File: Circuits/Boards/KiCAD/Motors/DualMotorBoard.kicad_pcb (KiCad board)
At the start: 2 copper layers, 127 x 101.6 mm, 124 parts, among them J1 Conn_01x05, J10 Conn_01x01, J11 Conn_01x01, J12 Conn_01x01, J13 Conn_01x01, J14 Conn_01x01, J15 Conn_01x02, J16 Conn_01x02, J17 MC34063, J2 Conn_01x01, J3 Conn_01x01, J4 Conn_01x01, J5 Conn_01x01, J6 Conn_01x01, J7 Conn_01x01, J8 Conn_01x05, J9 Conn_01x01, Q1 2N3904, Q10 Q_NMOS_DGS, Q11 Q_NMOS_DGS, Q12 Q_NMOS_DGS, Q13 Q_NMOS_DGS, Q14 2N3904, Q15 2N3904, Q16 2N3904, Q17 2N3904, Q18 2N3904, Q19 2N3904, Q2 2N3904, Q20 2N3904, Q21 2N3904, Q22 2N3904, Q23 Q_NMOS_DGS, Q24 Q_NMOS_DGS, Q25 Q_NMOS_DGS, Q26 Q_NMOS_DGS, Q3 2N3904, Q4 2N3904, Q5 2N3904, Q6 2N3904, Q7 2N3904, Q8 2N3904, Q9 2N3904, U2 LM7805_TO220

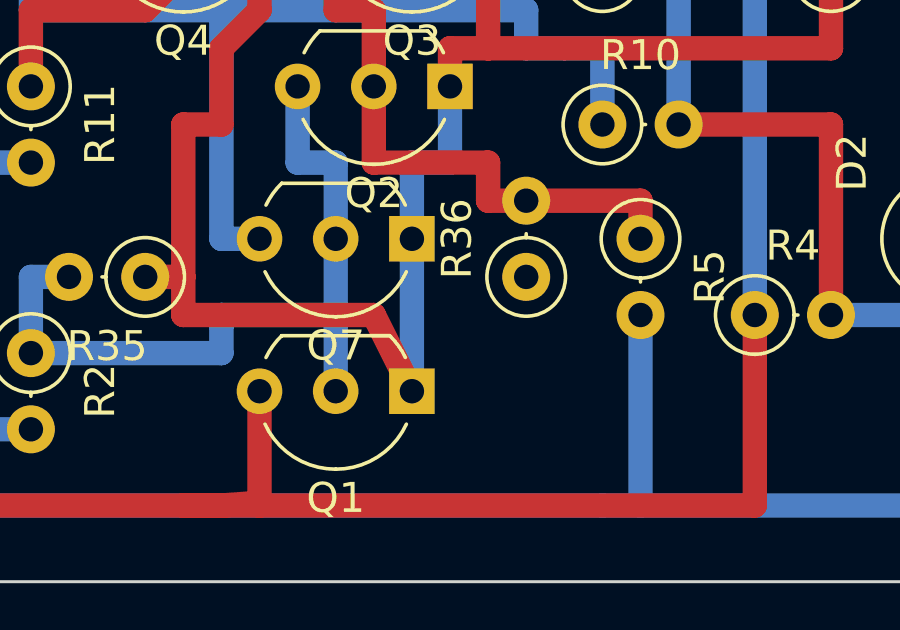
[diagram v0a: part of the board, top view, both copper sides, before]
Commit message: Fixed missing connections and routing errors
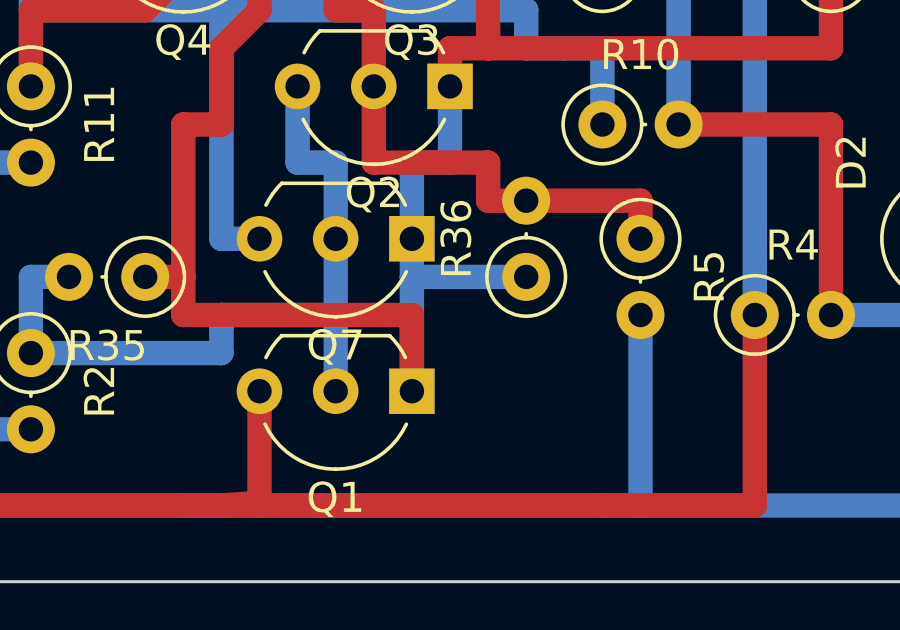
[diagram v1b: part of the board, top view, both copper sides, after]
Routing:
- net GND: track 605.8 -> 610.6 mm
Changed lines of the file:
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@@
   (general
     (links 255)
-    (no_connects 1)
+    (no_connects 0)
     (area 126.281 25.349999 254.819 127.549)
     (thickness 1.6)
     (drawings 4)
-    (tracks 543)
+    (tracks 546)
     (zones 0)
     (modules 124)
@@
   (segment (start 243.8 104.1) (end 242.57 102.87) (width 0.8128) (layer B.Cu) (net 1))
   (segment (start 250.19 101.6) (end 250.19 92.71) (width 0.8128) (layer B.Cu) (net 2))
+  (segment (start 223.52 118.11) (end 224.79 118.11) (width 0.8128) (layer F.Cu) (net 3))
+  (segment (start 224.79 118.11) (end 224.79 120.65) (width 0.8128) (layer F.Cu) (net 3))
+  (segment (start 228.6 116.84) (end 224.79 116.84) (width 0.8128) (layer B.Cu) (net 3))
   (segment (start 250.19 106.6) (end 238.84 106.6) (width 0.8128) (layer B.Cu) (net 3))
   (segment (start 238.84 106.6) (end 238.76 106.68) (width 0.8128) (layer B.Cu) (net 3))
@@
   (segment (start 215.9 116.84) (end 217.17 116.84) (width 0.8128) (layer F.Cu) (net 3))
   (segment (start 219.71 105.41) (end 219.71 107.95) (width 0.8128) (layer F.Cu) (net 3))
-  (segment (start 223.52 118.11) (end 224.79 120.65) (width 0.8128) (layer F.Cu) (net 3) (status 20))
   (segment (start 217.17 118.11) (end 223.52 118.11) (width 0.8128) (layer F.Cu) (net 3))
   (segment (start 217.17 111.76) (end 217.17 116.84) (width 0.8128) (layer F.Cu) (net 3))
@@
   (segment (start 218.44 109.22) (end 218.44 111.76) (width 0.8128) (layer F.Cu) (net 3))
   (segment (start 219.71 107.95) (end 218.44 109.22) (width 0.8128) (layer F.Cu) (net 3))
-  (segment (start 224.79 115.57) (end 224.79 120.65) (width 0.8128) (layer B.Cu) (net 3))
+  (segment (start 224.79 115.57) (end 224.79 116.84) (width 0.8128) (layer B.Cu) (net 3))
+  (segment (start 224.79 116.84) (end 224.79 120.65) (width 0.8128) (layer B.Cu) (net 3))
   (segment (start 214.63 62.23) (end 214.63 63.5) (width 0.8128) (layer B.Cu) (net 3))
   (segment (start 238.76 57.15) (end 247.65 57.15) (width 0.8128) (layer B.Cu) (net 3))
@@
   (segment (start 130.81 104.26) (end 137.04 104.26) (width 0.8128) (layer B.Cu) (net 48))
   (segment (start 137.04 104.26) (end 138.43 102.87) (width 0.8128) (layer B.Cu) (net 48))
-  (segment (start 201.93 116.84) (end 201.93 119.38) (width 1.27) (layer B.Cu) (net 49) (status 400000))
-  (segment (start 193.04 119.38) (end 193.04 121.92) (width 1.27) (layer B.Cu) (net 49) (status 800000))
+  (segment (start 201.93 116.84) (end 201.93 119.38) (width 1.27) (layer B.Cu) (net 49))
+  (segment (start 193.04 119.38) (end 193.04 121.92) (width 1.27) (layer B.Cu) (net 49))
   (segment (start 201.93 119.38) (end 193.04 119.38) (width 1.27) (layer B.Cu) (net 49))
-  (segment (start 195.54 121.92) (end 199.39 121.92) (width 1.27) (layer B.Cu) (net 50) (status C00000))
+  (segment (start 195.54 121.92) (end 199.39 121.92) (width 1.27) (layer B.Cu) (net 50))
   (segment (start 198.12 34.29) (end 198.12 34.29) (width 0.8128) (layer F.Cu) (net 51) (status 30))
   (segment (start 191.77 93.98) (end 194.31 93.98) (width 1.27) (layer F.Cu) (net 52))

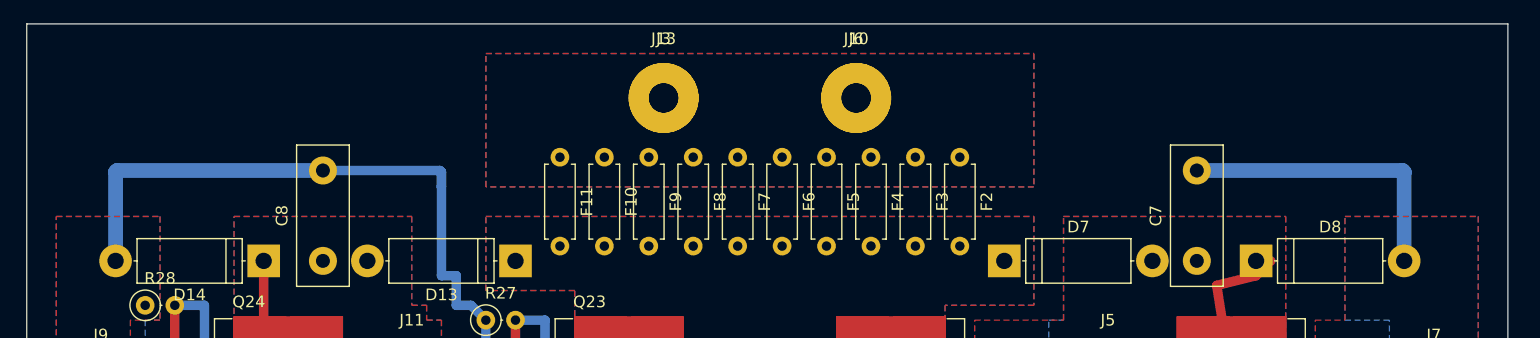
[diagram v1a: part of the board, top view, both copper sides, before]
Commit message: Added pin outputs for battery to ground (for external connections)
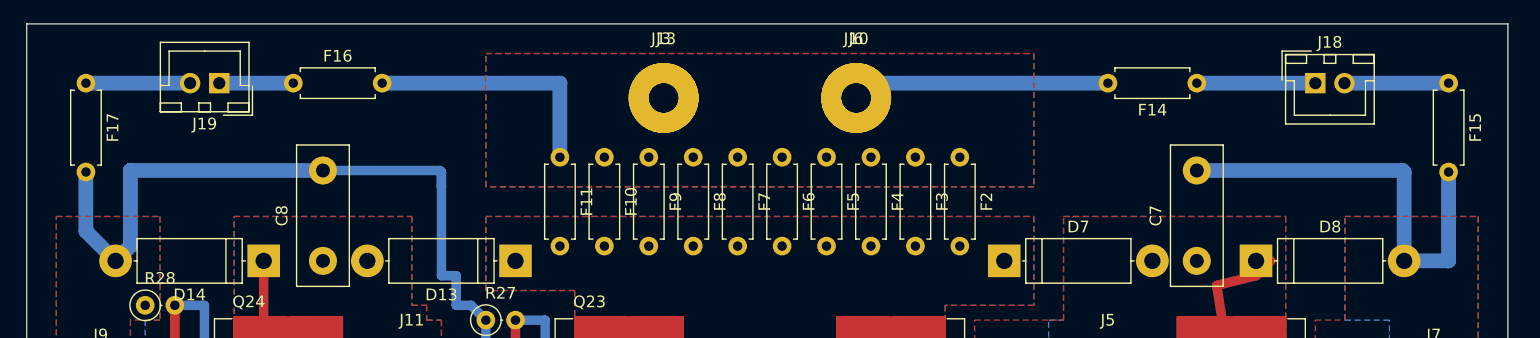
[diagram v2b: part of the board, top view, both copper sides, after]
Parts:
- added F14: Polyfuse, Resistors_THT:R_Axial_DIN0207_L6.3mm_D2.5mm_P7.62mm_Horizontal, F.Cu at (227.3, 30.5)
- added F15: Polyfuse, Resistors_THT:R_Axial_DIN0207_L6.3mm_D2.5mm_P7.62mm_Horizontal, F.Cu at (248.9, 30.5)
- added F16: Polyfuse, Resistors_THT:R_Axial_DIN0207_L6.3mm_D2.5mm_P7.62mm_Horizontal, F.Cu at (149.9, 30.5)
- added F17: Polyfuse, Resistors_THT:R_Axial_DIN0207_L6.3mm_D2.5mm_P7.62mm_Horizontal, F.Cu at (132.1, 30.5)
- added J18: Conn_01x02, Connectors_JST:JST_XH_B02B-XH-A_02x2.50mm_Straight, F.Cu at (237.5, 30.5)
- added J19: Conn_01x02, Connectors_JST:JST_XH_B02B-XH-A_02x2.50mm_Straight, F.Cu at (143.5, 30.5)
- C4: value 100uF -> 0.33uF
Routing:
- net +BATT: track 0.00 -> 43.7 mm
- net GND: track 610.6 -> 630.3 mm
- net Net-(F14-Pad1): track 0.00 -> 10.2 mm
- net Net-(F17-Pad1): track 0.00 -> 8.93 mm
- net Net-(F15-Pad1): track 0.00 -> 8.93 mm
- net Net-(F16-Pad1): track 0.00 -> 6.35 mm

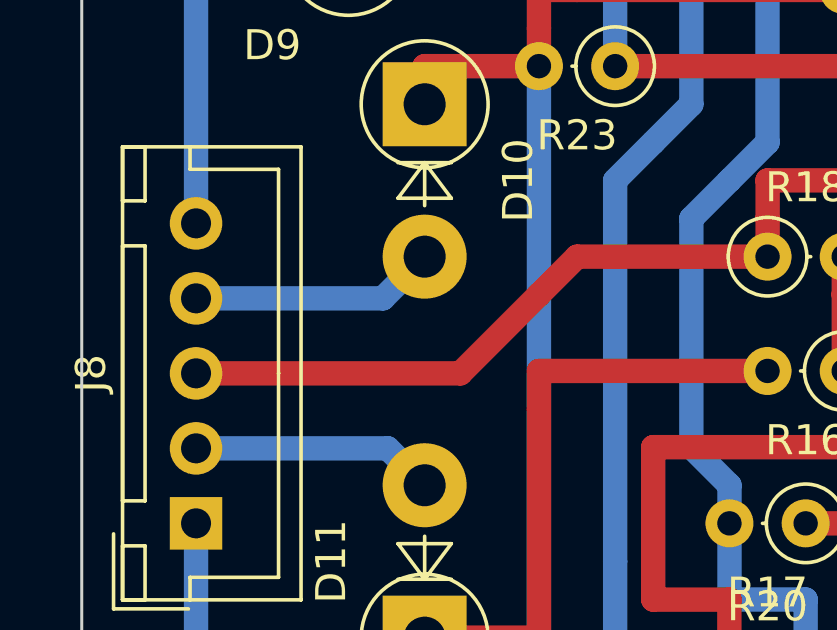
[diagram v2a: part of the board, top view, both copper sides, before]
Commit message: Transferred all JXT connections to bottomw traces
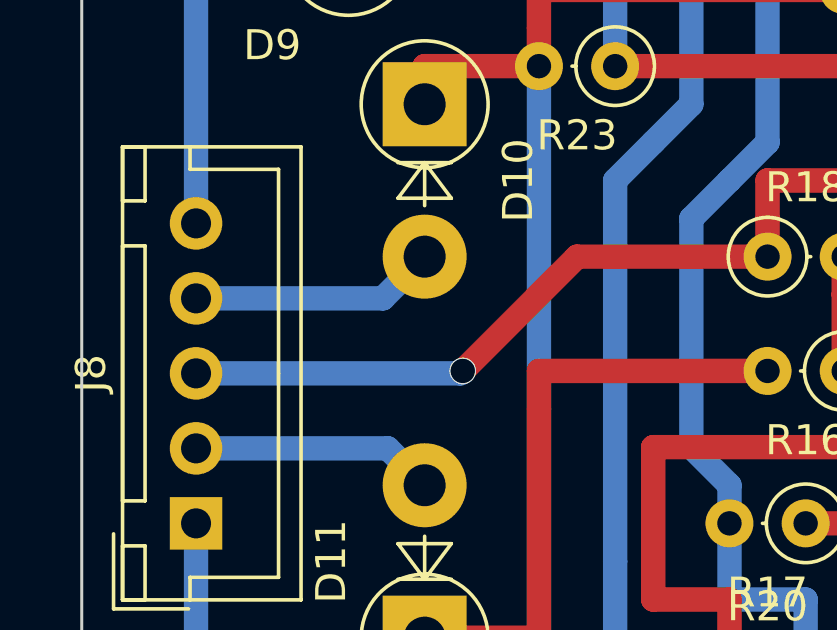
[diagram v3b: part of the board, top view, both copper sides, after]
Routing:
- net GND: vias 0 -> 1
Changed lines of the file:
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@@
     (thickness 1.6)
     (drawings 4)
-    (tracks 560)
+    (tracks 561)
     (zones 0)
     (modules 130)
@@
   (segment (start 243.8 104.1) (end 242.57 102.87) (width 0.8128) (layer B.Cu) (net 1))
   (segment (start 250.19 101.6) (end 250.19 92.71) (width 0.8128) (layer B.Cu) (net 2))
+  (segment (start 130.81 106.76) (end 139.62 106.76) (width 0.8128) (layer B.Cu) (net 3))
+  (segment (start 143.51 102.87) (end 149.86 102.87) (width 0.8128) (layer F.Cu) (net 3))
+  (segment (start 139.7 106.68) (end 143.51 102.87) (width 0.8128) (layer F.Cu) (net 3))
+  (via (at 139.7 106.68) (size 0.889) (drill 0.8128) (layers F.Cu B.Cu) (net 3))
+  (segment (start 139.62 106.76) (end 139.7 106.68) (width 0.8128) (layer B.Cu) (net 3))
   (segment (start 134.62 45.72) (end 135.89 44.45) (width 1.27) (layer B.Cu) (net 3))
   (segment (start 135.89 44.45) (end 135.89 37.97) (width 1.27) (layer B.Cu) (net 3))
@@
   (segment (start 149.86 101.6) (end 149.86 100.33) (width 0.8128) (layer F.Cu) (net 3))
   (segment (start 149.86 100.33) (end 153.67 100.33) (width 0.8128) (layer F.Cu) (net 3))
-  (segment (start 142.24 104.14) (end 143.51 102.87) (width 0.8128) (layer F.Cu) (net 3))
-  (segment (start 143.51 102.87) (end 149.86 102.87) (width 0.8128) (layer F.Cu) (net 3))
   (segment (start 158.75 121.92) (end 158.75 116.84) (width 0.8128) (layer F.Cu) (net 3) (status 10))
   (segment (start 161.29 111.76) (end 161.29 110.49) (width 0.8128) (layer F.Cu) (net 3))
@@
   (segment (start 179.15 105.41) (end 180.38 105.41) (width 1.27) (layer B.Cu) (net 3))
   (segment (start 179.11 105.37) (end 179.15 105.41) (width 1.27) (layer B.Cu) (net 3))
-  (segment (start 130.81 106.76) (end 139.62 106.76) (width 0.8128) (layer F.Cu) (net 3))
-  (segment (start 139.62 106.76) (end 142.24 104.14) (width 0.8128) (layer F.Cu) (net 3))
   (segment (start 160.02 102.87) (end 161.29 104.14) (width 0.8128) (layer F.Cu) (net 3))
   (segment (start 161.29 104.14) (end 162.56 104.14) (width 0.8128) (layer F.Cu) (net 3))
